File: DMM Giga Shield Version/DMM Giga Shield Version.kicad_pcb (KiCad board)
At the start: 4 copper layers, 95.6 x 53.3 mm, 77 parts, among them J10 ANALOG, J11 I_Input, J12 Conn_01x02_Pin, J13 DIGITAL1, J14 Barrel_Jack, J15 Barrel_Jack, J16 Conn_01x01_Socket, J17 Conn_01x01_Socket, J18 DIOs_Extended, J19 Conn_01x02_Pin, J21 Conn_02x18_Odd_Even, J4 A_Extended, J5 POWER2, J6 POWER1, J7 Conn_01x02_Pin, J8 DIGITAL2, J9 Out to Screen, Q1 MMBT3904, Q2 AO3400A MOSFET, Q6 BSS138, Q7 BSS138, Q8 AO3400A MOSFET, SW1 SW_Push, SW2 SW_Push, SW3 SW_SPDT, SW4 SW_Push, U1 LM317_TO-220, U10 LM4040DBZ-2.5, U11 LM4040DBZ-5, U12 TLV61046ADBVR, U2 IX4426N, U3 ADS1115IDGS, U4 IX4426N, U5 Opamp_Dual, U7 MAX1683, U8 Opamp_Dual, U9 TPS613222ADBV

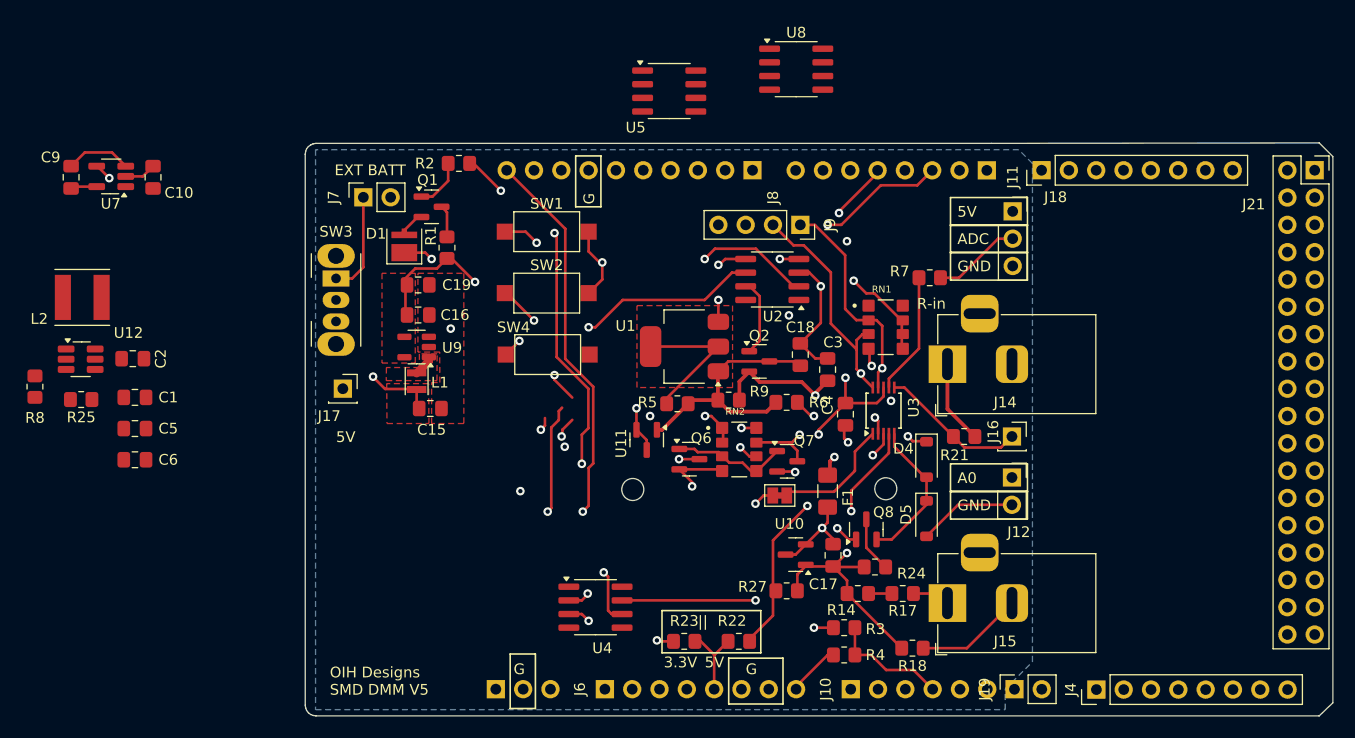
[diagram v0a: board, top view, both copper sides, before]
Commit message: Consolidated Data Sheets for used (or might use) components), PCB edits.
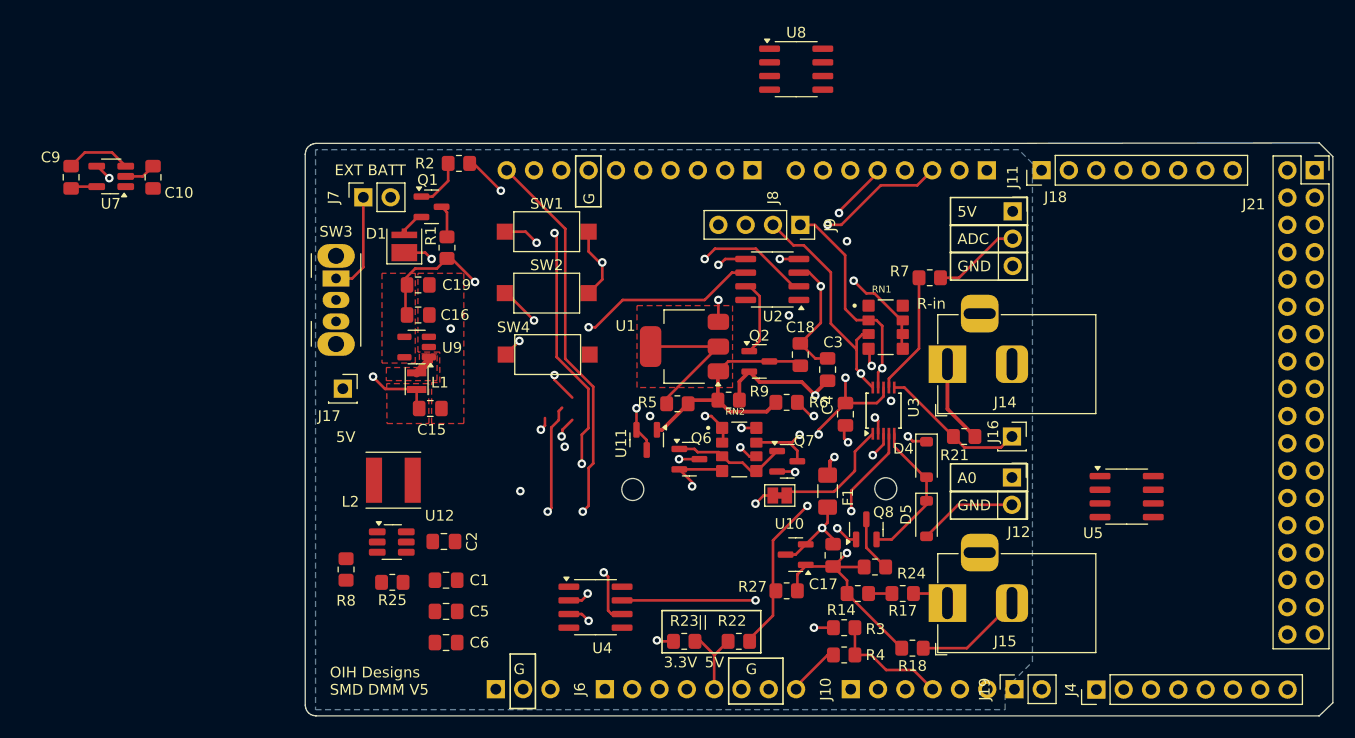
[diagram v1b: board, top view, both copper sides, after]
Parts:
- moved U5 56.9 mm to (154.8, 81.2)
- moved L2 33.6 mm to (86.6, 79.6)
- moved C1 33.6 mm to (91.5, 88.9)
- moved C5 33.6 mm to (91.5, 91.8)
- moved C6 33.6 mm to (91.5, 94.7)
- moved R25 33.6 mm to (86.5, 89.1)
- moved R8 33.6 mm to (82.2, 87.9)
- moved U12 33.6 mm to (86.5, 85.4)
- moved C2 33.6 mm to (91.3, 85.3)
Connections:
- U5 pad 1: unconnected-(U5-Pad1) -> Net-(U5A--)
- U5 pad 2: unconnected-(U5A---Pad2) -> Net-(U5A--)
- U5 pad 3: unconnected-(U5A-+-Pad3) -> DAC1
- U5 pad 4: unconnected-(U5C-V--Pad4) -> GND
- U5 pad 8: unconnected-(U5C-V+-Pad8) -> VDD
